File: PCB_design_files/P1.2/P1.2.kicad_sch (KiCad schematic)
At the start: 32 parts, among them J1 -EEG_INPUT, J2 +EEG_INPUT, J3 +3.3V, J4 GND, U1 INA819, U2 TPS61094, U4 TC1044

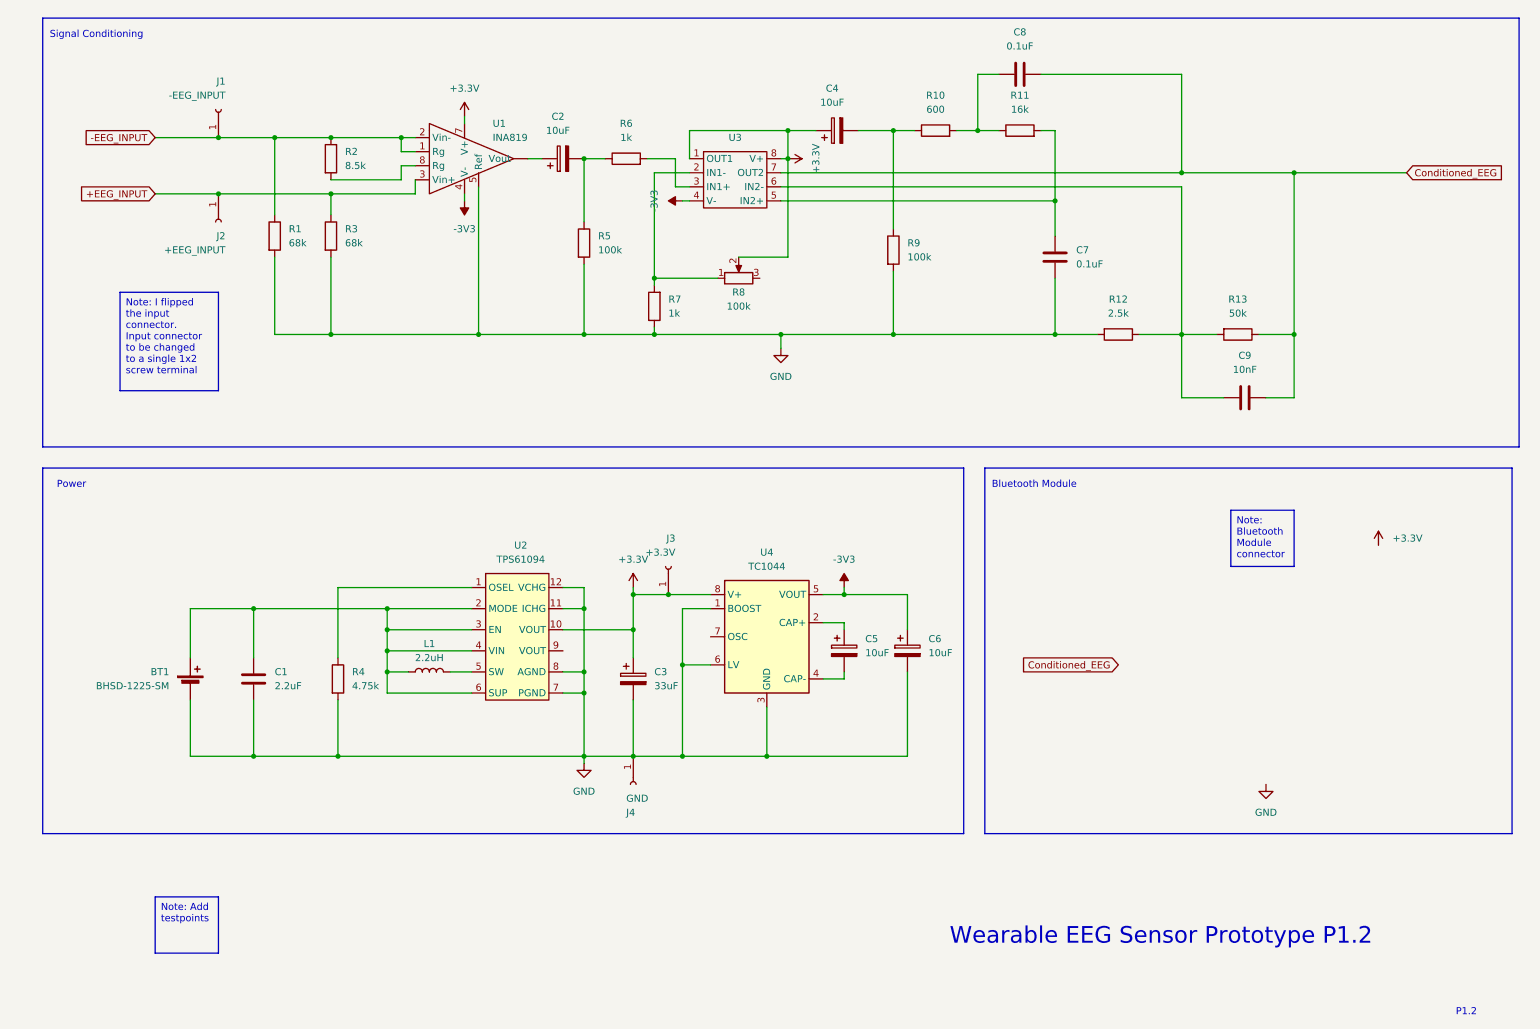
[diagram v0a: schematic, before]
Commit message: Added footprints for existing components
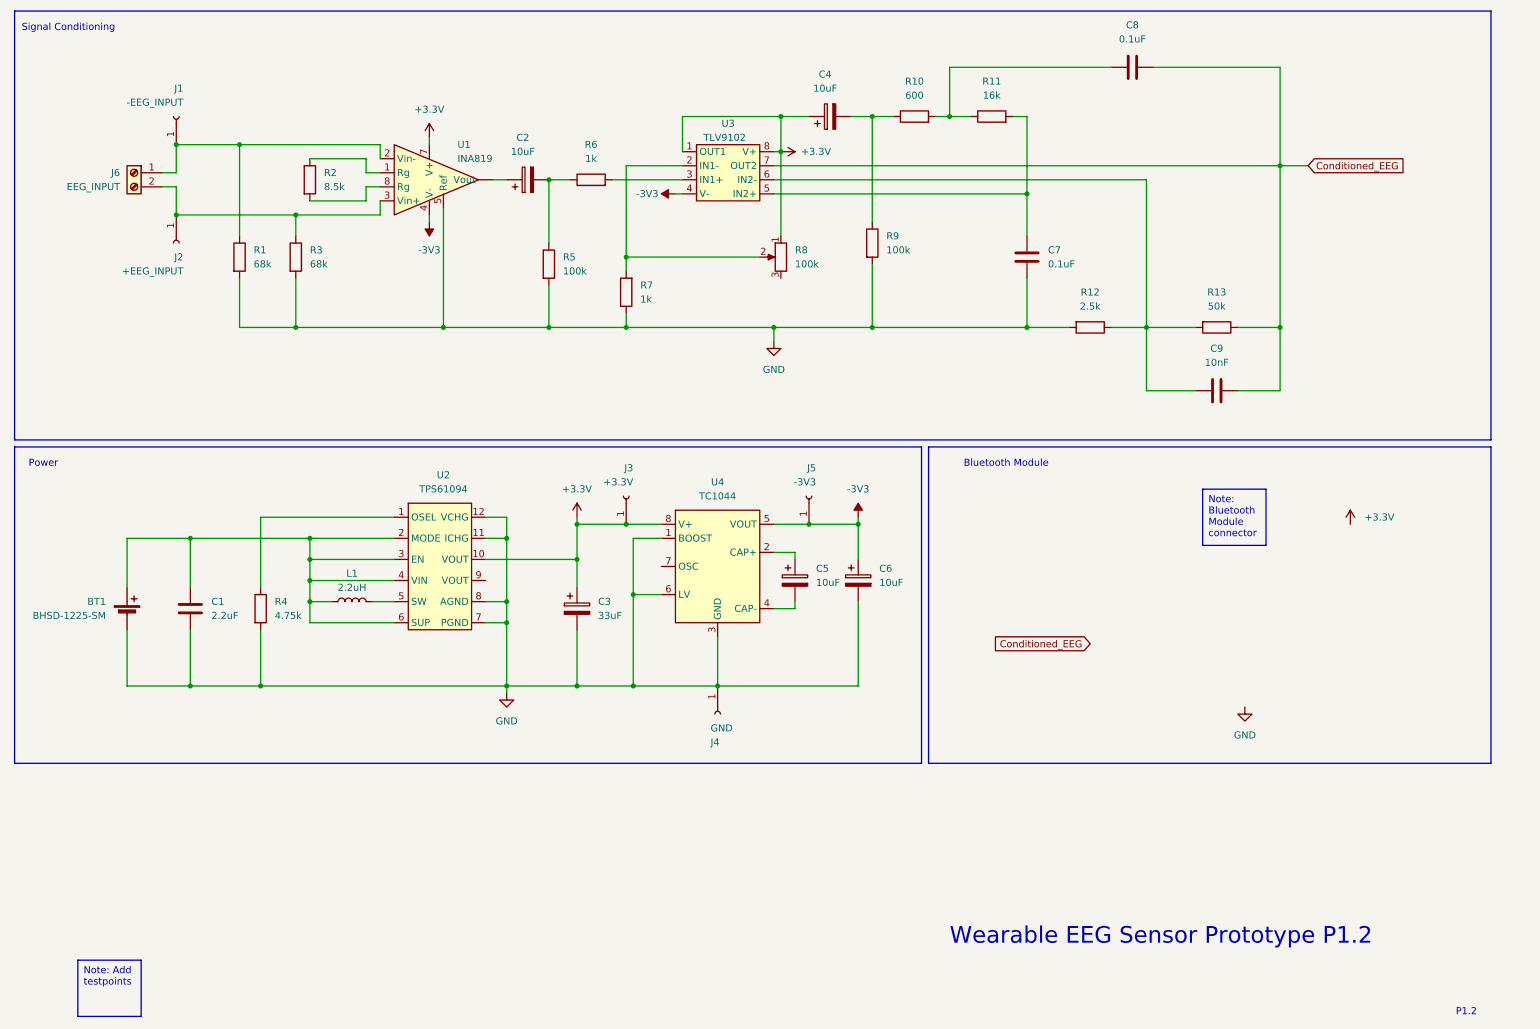
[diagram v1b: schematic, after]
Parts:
- added J5: -3V3, TestPoint:TestPoint_Loop_D2.50mm_Drill1.0mm, symbol Connector:Conn_01x01_Socket
- added J6: EEG_INPUT, 282837-2:282837-2_TYC, symbol Connector:Screw_Terminal_01x02
- BT1: footprint (none) -> BHSD-1225-SM:BAT_BHSD-1225-SM
- J1, J2, J3, J4: footprint (none) -> TestPoint:TestPoint_Loop_D2.50mm_Drill1.0mm
- L1: footprint (none) -> B78108S1222K000:INDAD1400W80L920D400
- U1, U4: footprint (none) -> 1-2199298-2:CONN8_1-2199298-2_TEC
- U2: footprint (none) -> TPS61094DSSR:WSON_94DSSR_TEX
- U3: value ~ -> TLV9102; footprint (none) -> 1-2199298-2:CONN8_1-2199298-2_TEC
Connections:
- net +3.3V: now also R8.1; no longer R8.2
- net -3V3: now also J5.1 (Pin_1)
- net at R7.2, U3.2 (IN1-): now also R8.2; no longer R8.1
- net +EEG_INPUT: no longer names the net of J2.1 (Pin_1), R3.1, U1.3 (Vin+)
- net +EEG_INPUT: now also J6.2 (Pin_2)
- net -EEG_INPUT: no longer names the net of J1.1 (Pin_1), R1.1, U1.2 (Vin-)
- net -EEG_INPUT: now also J6.1 (Pin_1); no longer R2.1, U1.1 (Rg)
- new net: R2.1, U1.1 (Rg)
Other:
- moved on the sheet: BT1, C1, C2, C3, C4, C5, C6, C7, C8, C9, J1, J2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

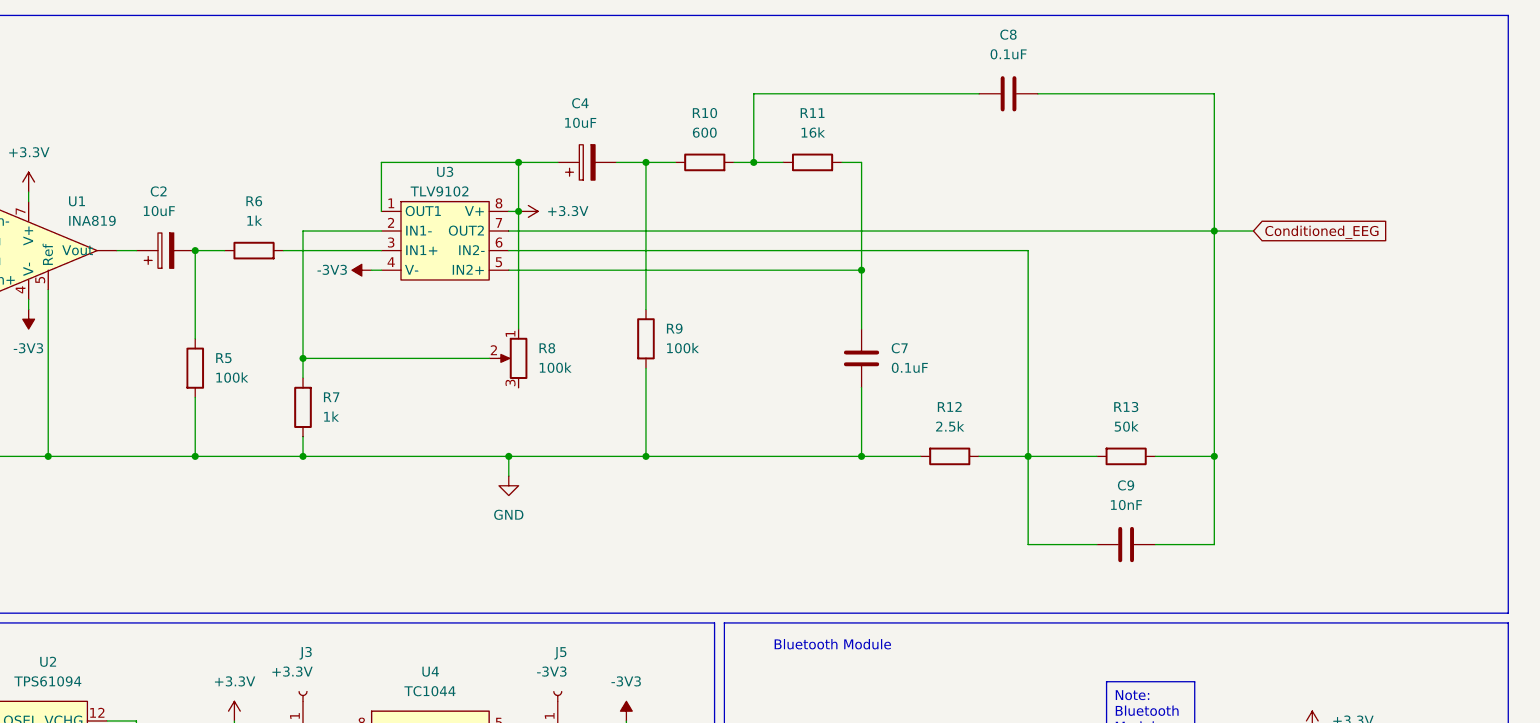
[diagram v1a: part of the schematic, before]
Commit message: added some testpoints
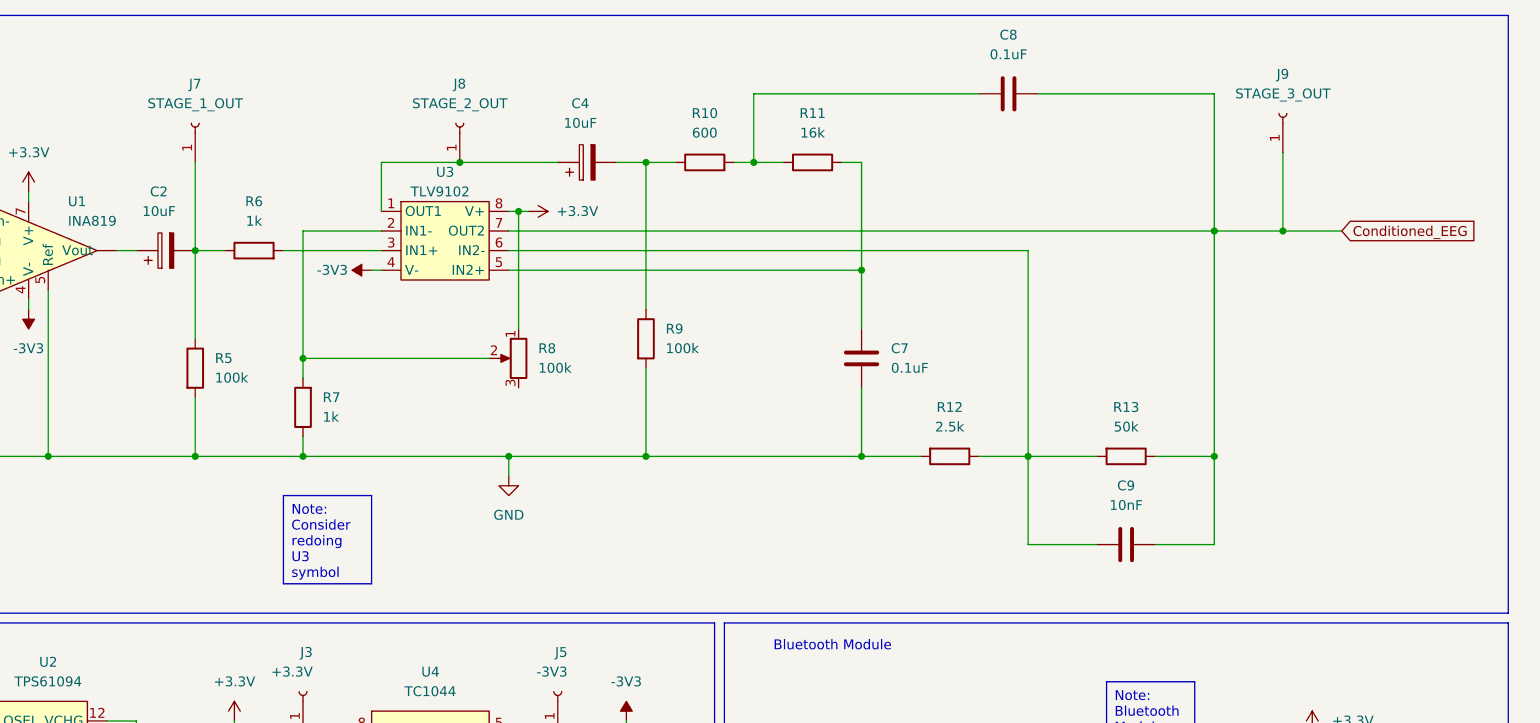
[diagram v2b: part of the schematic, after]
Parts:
- added J7: STAGE_1_OUT, TestPoint:TestPoint_Loop_D2.50mm_Drill1.0mm, symbol Connector:Conn_01x01_Socket
- added J8: STAGE_2_OUT, TestPoint:TestPoint_Loop_D2.50mm_Drill1.0mm, symbol Connector:Conn_01x01_Socket
- added J9: STAGE_3_OUT, TestPoint:TestPoint_Loop_D2.50mm_Drill1.0mm, symbol Connector:Conn_01x01_Socket
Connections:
- net +3.3V: no longer C4.1, U3.1 (OUT1)
- net Conditioned_EEG: now also J9.1 (Pin_1)
- net at C2.2, R5.1, R6.1: now also J7.1 (Pin_1)
- new net: C4.1, J8.1 (Pin_1), U3.1 (OUT1)
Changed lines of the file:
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@@
   (junction (at 57.15 134.62) (diameter 0) (color 0 0 0 0)
   )
-  (junction (at 151.13 31.75) (diameter 0) (color 0 0 0 0)
+  (junction (at 143.51 31.75) (diameter 0) (color 0 0 0 0)
   )
   (junction (at 124.46 118.11) (diameter 0) (color 0 0 0 0)
   )
+  (junction (at 250.19 40.64) (diameter 0) (color 0 0 0 0)
+  )
   (junction (at 41.91 36.83) (diameter 0) (color 0 0 0 0)
   )
@@
   (junction (at 41.91 49.53) (diameter 0) (color 0 0 0 0)
   )
-  (wire (pts (xy 151.13 31.75) (xy 156.21 31.75))
-    (stroke (width 0) (type default))
-  )
-  (wire (pts (xy 133.35 31.75) (xy 151.13 31.75))
+  (wire (pts (xy 133.35 31.75) (xy 143.51 31.75))
     (stroke (width 0) (type default))
   )
@@
     (stroke (width 0) (type default))
   )
+  (wire (pts (xy 241.3 22.86) (xy 241.3 40.64))
+    (stroke (width 0) (type default))
+  )
   (wire (pts (xy 139.7 125.73) (xy 139.7 134.62))
     (stroke (width 0) (type default))
@@
     (stroke (width 0) (type default))
   )
-  (wire (pts (xy 241.3 40.64) (xy 241.3 22.86))
-    (stroke (width 0) (type default))
-  )
   (wire (pts (xy 195.58 31.75) (xy 195.58 45.72))
     (stroke (width 0) (type default))
@@
     (stroke (width 0) (type default))
   )
-  (wire (pts (xy 151.13 31.75) (xy 151.13 38.1))
+  (wire (pts (xy 250.19 30.48) (xy 250.19 40.64))
     (stroke (width 0) (type default))
   )
@@
     (stroke (width 0) (type default))
   )
+  (wire (pts (xy 109.22 31.75) (xy 109.22 43.18))
+    (stroke (width 0) (type default))
+  )
   (wire (pts (xy 124.46 118.11) (xy 124.46 134.62))
     (stroke (width 0) (type default))
@@
     (stroke (width 0) (type default))
   )
+  (wire (pts (xy 143.51 31.75) (xy 156.21 31.75))
+    (stroke (width 0) (type default))
+  )
   (wire (pts (xy 66.04 123.19) (xy 66.04 119.38))
     (stroke (width 0) (type default))
@@
     (stroke (width 0) (type default))
   )
+  (wire (pts (xy 250.19 40.64) (xy 257.81 40.64))
+    (stroke (width 0) (type default))
+  )
   (wire (pts (xy 57.15 124.46) (xy 57.15 134.62))
     (stroke (width 0) (type default))
@@
     (stroke (width 0) (type default))
   )
-  (wire (pts (xy 241.3 40.64) (xy 246.38 40.64))
+  (wire (pts (xy 241.3 40.64) (xy 250.19 40.64))
     (stroke (width 0) (type default))
   )
@@
     (stroke (width 0) (type default))
   )
+  (wire (pts (xy 152.4 38.1) (xy 151.13 38.1))
+    (stroke (width 0) (type default))
+  )
   (wire (pts (xy 123.19 57.15) (xy 147.32 57.15))
     (stroke (width 0) (type default))
@@
     (stroke (width 0) (type default))
     (fill (type none))
+  )
+  (text_box "Note: Consider redoing U3 symbol"
+    (at 120.65 74.93 0) (size 11.43 11.43)
+    (stroke (width 0) (type default))
+    (fill (type color) (color 255 215 209 1))
+    (effects (font (size 1.27 1.27)) (justify left top))
   )
   (text_box "Note: Add testpoints"
@@
     )
   )
-  (global_label "Conditioned_EEG" (shape input) (at 246.38 40.64 0) (fields_autoplaced)
+  (global_label "Conditioned_EEG" (shape input) (at 257.81 40.64 0) (fields_autoplaced)
     (effects (font (size 1.27 1.27)) (justify left))
-    (property "Intersheetrefs" "${INTERSHEET_REFS}" (at 265.0887 40.64 0)
+    (property "Intersheetrefs" "${INTERSHEET_REFS}" (at 276.5187 40.64 0)
       (effects (font (size 1.27 1.27)) (justify left) hide)
     )
@@
         (path "/14ccd594-9acb-4c8c-856d-2255d639ffb5"
           (reference "#PWR04") (unit 1)
+        )
+      )
+    )
+  )
+  (symbol (lib_id "Connector:Conn_01x01_Socket") (at 143.51 26.67 270) (mirror x) (unit 1)
+    (in_bom yes) (on_board yes) (dnp no)
+    (property "Reference" "J8" (at 143.51 21.59 90)
+      (effects (font (size 1.27 1.27)))
+    )
+    (property "Value" "STAGE_2_OUT" (at 143.51 24.13 90)
+      (effects (font (size 1.27 1.27)))
+    )
+    (property "Footprint" "TestPoint:TestPoint_Loop_D2.50mm_Drill1.0mm" (at 143.51 26.67 0)
+      (effects (font (size 1.27 1.27)) hide)
+    )
+    (property "Datasheet" "~" (at 143.51 26.67 0)
+      (effects (font (size 1.27 1.27)) hide)
+    )
+    (pin "1")
+    (instances
+      (project "P1.2"
+        (path "/14ccd594-9acb-4c8c-856d-2255d639ffb5"
+          (reference "J8") (unit 1)
+        )
+      )
+      (project "Capstone"
+        (path "/dd9861b4-b57a-4b4e-bd42-9d4b17c05a17"
+          (reference "J1") (unit 1)
         )
       )
@@
     )
   )
+  (symbol (lib_id "Connector:Conn_01x01_Socket") (at 109.22 26.67 270) (mirror x) (unit 1)
+    (in_bom yes) (on_board yes) (dnp no)
+    (property "Reference" "J7" (at 109.22 21.59 90)
+      (effects (font (size 1.27 1.27)))
+    )
+    (property "Value" "STAGE_1_OUT" (at 109.22 24.13 90)
+      (effects (font (size 1.27 1.27)))
+    )
+    (property "Footprint" "TestPoint:TestPoint_Loop_D2.50mm_Drill1.0mm" (at 109.22 26.67 0)
+      (effects (font (size 1.27 1.27)) hide)
+    )
+    (property "Datasheet" "~" (at 109.22 26.67 0)
+      (effects (font (size 1.27 1.27)) hide)
+    )
+    (pin "1")
+    (instances
+      (project "P1.2"
+        (path "/14ccd594-9acb-4c8c-856d-2255d639ffb5"
+          (reference "J7") (unit 1)
+        )
+      )
+      (project "Capstone"
+        (path "/dd9861b4-b57a-4b4e-bd42-9d4b17c05a17"
+          (reference "J1") (unit 1)
+        )
+      )
+    )
+  )
   (symbol (lib_id "Device:R_Potentiometer") (at 151.13 57.15 0) (mirror y) (unit 1)
     (in_bom yes) (on_board yes) (dnp no)
@@
     )
   )
+  (symbol (lib_id "Connector:Conn_01x01_Socket") (at 250.19 25.4 270) (mirror x) (unit 1)
+    (in_bom yes) (on_board yes) (dnp no)
+    (property "Reference" "J9" (at 250.19 20.32 90)
+      (effects (font (size 1.27 1.27)))
+    )
+    (property "Value" "STAGE_3_OUT" (at 250.19 22.86 90)
+      (effects (font (size 1.27 1.27)))
+    )
+    (property "Footprint" "TestPoint:TestPoint_Loop_D2.50mm_Drill1.0mm" (at 250.19 25.4 0)
+      (effects (font (size 1.27 1.27)) hide)
+    )
+    (property "Datasheet" "~" (at 250.19 25.4 0)
+      (effects (font (size 1.27 1.27)) hide)
+    )
+    (pin "1")
+    (instances
+      (project "P1.2"
+        (path "/14ccd594-9acb-4c8c-856d-2255d639ffb5"
+          (reference "J9") (unit 1)
+        )
+      )
+      (project "Capstone"
+        (path "/dd9861b4-b57a-4b4e-bd42-9d4b17c05a17"
+          (reference "J1") (unit 1)
+        )
+      )
+    )
+  )
   (symbol (lib_id "Device:R") (at 63.5 57.15 0) (unit 1)
     (in_bom yes) (on_board yes) (dnp no) (fields_autoplaced)
@@
     )
   )
-  (symbol (lib_id "power:+3.3V") (at 151.13 38.1 270) (unit 1)
+  (symbol (lib_id "power:+3.3V") (at 152.4 38.1 270) (unit 1)
     (in_bom yes) (on_board yes) (dnp no)
-    (property "Reference" "#PWR05" (at 147.32 38.1 0)
-      (effects (font (size 1.27 1.27)) hide)
-    )
-    (property "Value" "+3.3V" (at 157.48 38.1 90)
-      (effects (font (size 1.27 1.27)))
-    )
-    (property "Footprint" "" (at 151.13 38.1 0)
-      (effects (font (size 1.27 1.27)) hide)
-    )
-    (property "Datasheet" "" (at 151.13 38.1 0)
-      (effects (font (size 1.27 1.27)) hide)
-    )
+    (property "Reference" "#PWR05" (at 148.59 38.1 0)
+      (effects (font (size 1.27 1.27)) hide)
+    )
+    (property "Value" "+3.3V" (at 158.75 38.1 90)
+      (effects (font (size 1.27 1.27)))
+    )
+    (property "Footprint" "" (at 152.4 38.1 0)
+      (effects (font (size 1.27 1.27)) hide)
+    )
+    (property "Datasheet" "" (at 152.4 38.1 0)
+      (effects (font (size 1.27 1.27)) hide)
+    )
